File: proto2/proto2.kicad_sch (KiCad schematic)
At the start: 9 parts, among them J12 Daughter Card, SW1 SW_DIP_x04

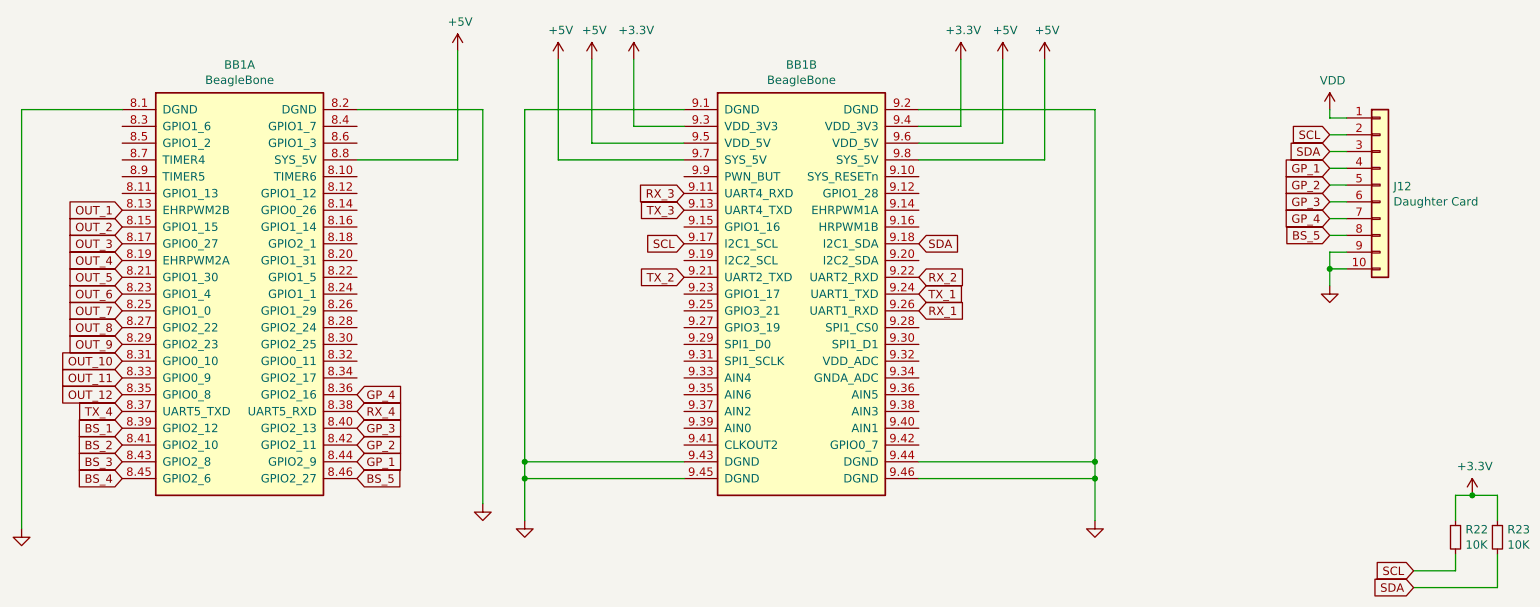
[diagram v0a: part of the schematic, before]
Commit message: Added another 2 outputs and re-routed board.
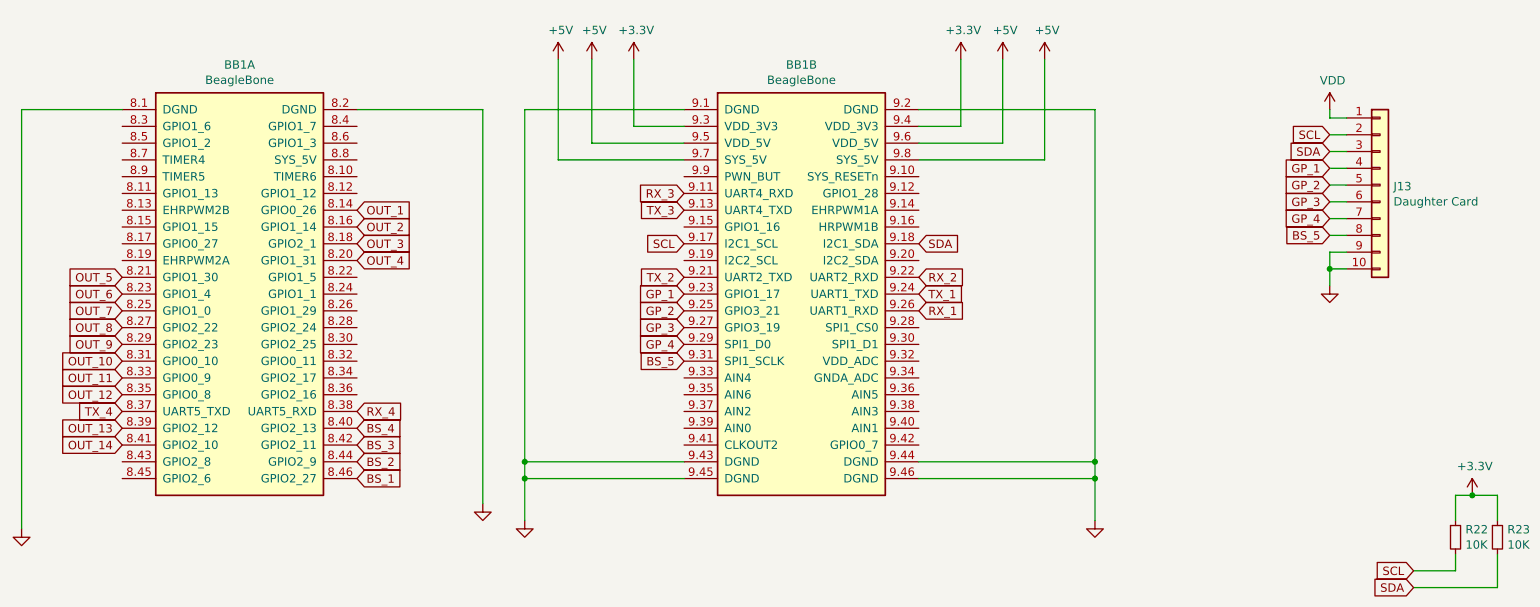
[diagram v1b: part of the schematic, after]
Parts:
- renumbered J12 to J13
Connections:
- net +5V: no longer BB1.8.8 (SYS_5V)
- net BS_1: now also BB1.8.46 (GPIO2_27); no longer BB1.8.39 (GPIO2_12)
- net BS_2: now also BB1.8.44 (GPIO2_9); no longer BB1.8.41 (GPIO2_10)
- net BS_3: now also BB1.8.42 (GPIO2_11); no longer BB1.8.43 (GPIO2_8)
- net BS_4: now also BB1.8.40 (GPIO2_13); no longer BB1.8.45 (GPIO2_6)
- net BS_5: now also BB1.9.31 (SPI1_SCLK); no longer BB1.8.46 (GPIO2_27)
- net GP_1: now also BB1.9.23 (GPIO1_17); no longer BB1.8.44 (GPIO2_9)
- net GP_2: now also BB1.9.25 (GPIO3_21); no longer BB1.8.42 (GPIO2_11)
- net GP_3: now also BB1.9.27 (GPIO3_19); no longer BB1.8.40 (GPIO2_13)
- net GP_4: now also BB1.9.29 (SPI1_D0); no longer BB1.8.36 (GPIO2_16)
- net OUT_1: now also BB1.8.14 (GPIO0_26); no longer BB1.8.13 (EHRPWM2B)
- net OUT_2: now also BB1.8.16 (GPIO1_14); no longer BB1.8.15 (GPIO1_15)
- net OUT_3: now also BB1.8.18 (GPIO2_1); no longer BB1.8.17 (GPIO0_27)
- net OUT_4: now also BB1.8.20 (GPIO1_31); no longer BB1.8.19 (EHRPWM2A)
- new net OUT_13: BB1.8.39 (GPIO2_12)
- new net OUT_14: BB1.8.41 (GPIO2_10)

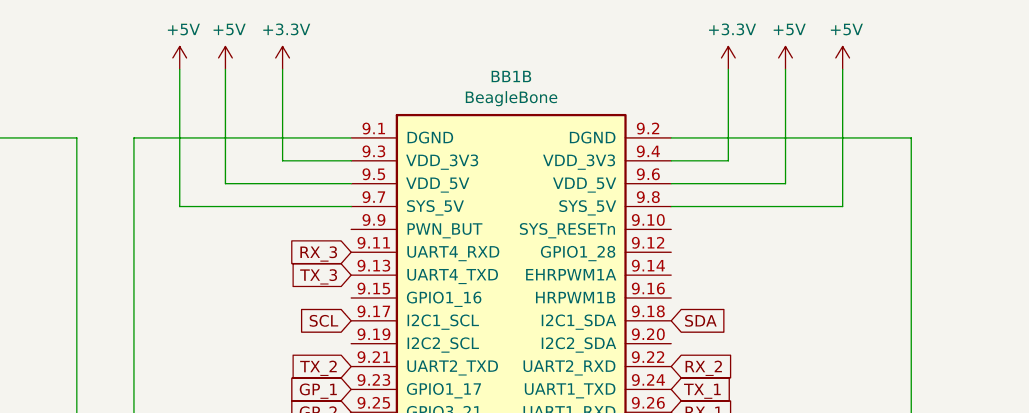
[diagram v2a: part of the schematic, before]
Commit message: Added switch for 5V external devices power based off SYS_RESETn.
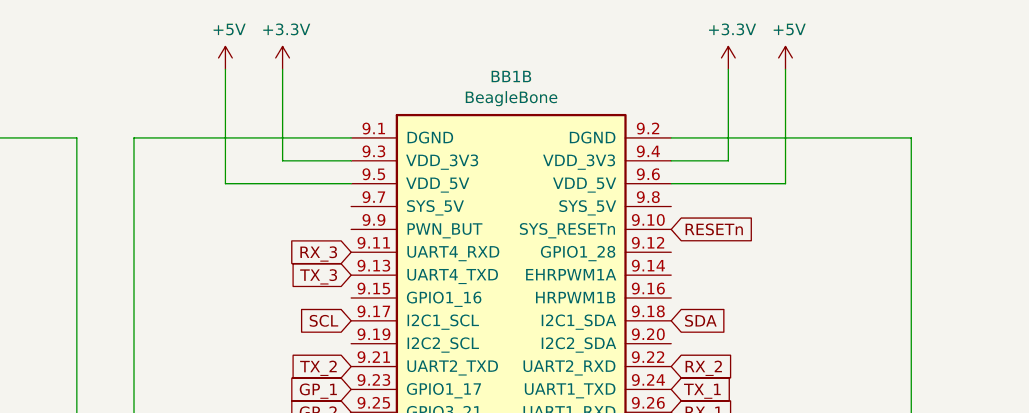
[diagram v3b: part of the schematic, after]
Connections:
- net +5V: no longer BB1.9.7 (SYS_5V), BB1.9.8 (SYS_5V)
- net RESETn: now reaches BB1.9.10 (SYS_RESETn)
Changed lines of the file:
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@@
-    (stroke (width 0) (type default) (color 0 0 0 0))
-  )
-  (wire (pts (xy 160.02 40.64) (xy 179.07 40.64))
     (stroke (width 0) (type default) (color 0 0 0 0))
   )
@@
     (stroke (width 0) (type default) (color 0 0 0 0))
   )
-  (wire (pts (xy 124.46 40.64) (xy 105.41 40.64))
-    (stroke (width 0) (type default) (color 0 0 0 0))
-  )
   (wire (pts (xy 224.79 36.83) (xy 222.25 36.83))
     (stroke (width 0) (type default) (color 0 0 0 0))
@@
     (stroke (width 0) (type default) (color 0 0 0 0))
   )
-  (wire (pts (xy 105.41 25.4) (xy 105.41 40.64))
-    (stroke (width 0) (type default) (color 0 0 0 0))
-  )
   (wire (pts (xy 193.04 137.16) (xy 198.12 137.16))
     (stroke (width 0) (type default) (color 0 0 0 0))
@@
   )
   (wire (pts (xy 214.63 125.73) (xy 214.63 120.65))
-    (stroke (width 0) (type default) (color 0 0 0 0))
-  )
-  (wire (pts (xy 179.07 40.64) (xy 179.07 25.4))
     (stroke (width 0) (type default) (color 0 0 0 0))
   )
@@
     (property "Intersheet References" "${INTERSHEET_REFS}" (id 0) (at 0 0 0)
       (effects (font (size 1.27 1.27)) hide)
+    )
+  )
+  (global_label "RESETn" (shape input) (at 160.02 43.18 0) (fields_autoplaced)
+    (effects (font (size 1.27 1.27)) (justify left))
+    (property "Intersheet References" "${INTERSHEET_REFS}" (id 0) (at 169.2385 43.1006 0)
+      (effects (font (size 1.27 1.27)) (justify left) hide)
     )
   )
@@
     (pin "1")
   )
-  (symbol (lib_id "power:+5V") (at 179.07 25.4 0) (unit 1)
-    (in_bom yes) (on_board yes)
-    (property "Reference" "#PWR07" (id 0) (at 179.07 29.21 0)
-      (effects (font (size 1.27 1.27)) hide)
-    )
-    (property "Value" "+5V" (id 1) (at 179.451 21.0058 0))
-    (property "Footprint" "" (id 2) (at 179.07 25.4 0)
-      (effects (font (size 1.27 1.27)) hide)
-    )
-    (property "Datasheet" "" (id 3) (at 179.07 25.4 0)
-      (effects (font (size 1.27 1.27)) hide)
-    )
-    (pin "1")
-  )
   (symbol (lib_id "power:+5V") (at 110.49 25.4 0) (unit 1)
     (in_bom yes) (on_board yes)
@@
     )
     (property "Datasheet" "" (id 3) (at 110.49 25.4 0)
-      (effects (font (size 1.27 1.27)) hide)
-    )
-    (pin "1")
-  )
-  (symbol (lib_id "power:+5V") (at 105.41 25.4 0) (unit 1)
-    (in_bom yes) (on_board yes)
-    (property "Reference" "#PWR02" (id 0) (at 105.41 29.21 0)
-      (effects (font (size 1.27 1.27)) hide)
-    )
-    (property "Value" "+5V" (id 1) (at 105.791 21.0058 0))
-    (property "Footprint" "" (id 2) (at 105.41 25.4 0)
-      (effects (font (size 1.27 1.27)) hide)
-    )
-    (property "Datasheet" "" (id 3) (at 105.41 25.4 0)
       (effects (font (size 1.27 1.27)) hide)
     )
@@
   )
   (symbol_instances
-    (path "/00000000-0000-0000-0000-000061bf4728"
-      (reference "#PWR02") (unit 1) (value "+5V") (footprint "")
+    (path "/00000000-0000-0000-0000-0000619eb672/a2db9d7b-b7f0-42c4-8bfa-d906fa3f908d"
+      (reference "#PWR01") (unit 1) (value "+5V") (footprint "")
+    )
+    (path "/00000000-0000-0000-0000-0000619eb672/1ea60411-14df-4e7e-a9fa-3b3b00f1524d"
+      (reference "#PWR02") (unit 1) (value "GND") (footprint "")
     )
     (path "/00000000-0000-0000-0000-000061bf42fc"
@@
       (reference "#PWR06") (unit 1) (value "+5V") (footprint "")
     )
-    (path "/00000000-0000-0000-0000-000061bf4113"
+    (path "/00000000-0000-0000-0000-0000619eb672/eaa45e24-ca48-404a-92a9-31cfd5b343bc"
       (reference "#PWR07") (unit 1) (value "+5V") (footprint "")
     )
@@
       (reference "#PWR079") (unit 1) (value "GNDPWR") (footprint "")
     )
+    (path "/00000000-0000-0000-0000-0000619eb672/e7637630-81e1-4c33-8f3d-d08d1824d6f6"
+      (reference "#PWR080") (unit 1) (value "+5VP") (footprint "")
+    )
     (path "/00000000-0000-0000-0000-0000619eb672/00000000-0000-0000-0000-000061cae676"
       (reference "#PWR096") (unit 1) (value "GNDPWR") (footprint "")
@@
       (reference "#PWR0109") (unit 1) (value "VDD") (footprint "")
     )
-    (path "/00000000-0000-0000-0000-0000619eb672/00000000-0000-0000-0000-000061daa2a5"
-      (reference "#PWR0110") (unit 1) (value "+5V") (footprint "")
-    )
     (path "/00000000-0000-0000-0000-0000619eb672/00000000-0000-0000-0000-000061ba8e74"
       (reference "#PWR0111") (unit 1) (value "GND") (footprint "")
@@
       (reference "#PWR0165") (unit 1) (value "Earth") (footprint "")
     )
+    (path "/00000000-0000-0000-0000-0000619eb672/b6c5cff6-cf86-4498-a76d-b9f56c83bf6b"
+      (reference "#PWR?") (unit 1) (value "+5VP") (footprint "")
+    )
     (path "/00000000-0000-0000-0000-000061b4e58b"
       (reference "BB1") (unit 1) (value "BeagleBone") (footprint "BCR_SBC:BeagleBone_UpsideDown")
@@
       (reference "Q14") (unit 1) (value "2N7002") (footprint "Package_TO_SOT_SMD:SOT-23")
     )
+    (path "/00000000-0000-0000-0000-0000619eb672/b660b5f4-a97d-4cf0-a5cf-f1705548cf79"
+      (reference "Q15") (unit 1) (value "2N7002") (footprint "Package_TO_SOT_SMD:SOT-23")
+    )
     (path "/00000000-0000-0000-0000-000061c509a6"
       (reference "R1") (unit 1) (value "10K") (footprint "Resistor_SMD:R_0805_2012Metric")
@@
       (reference "R54") (unit 1) (value "500R") (footprint "Capacitor_SMD:C_0805_2012Metric")
     )
+    (path "/00000000-0000-0000-0000-0000619eb672/5b1cfd4b-7b06-4f3f-8036-d9ad45660df3"
+      (reference "R55") (unit 1) (value "1K") (footprint "Resistor_SMD:R_0805_2012Metric")
+    )
+    (path "/00000000-0000-0000-0000-0000619eb672/22fe218f-cd70-40d4-84da-5b3454bd320a"
+      (reference "R56") (unit 1) (value "27K") (footprint "Resistor_SMD:R_0805_2012Metric")
+    )
+    (path "/00000000-0000-0000-0000-0000619eb672/ead9c149-9ccc-4416-b4a2-f88d2a070289"
+      (reference "R57") (unit 1) (value "433R") (footprint "Resistor_SMD:R_0805_2012Metric")
+    )
     (path "/00000000-0000-0000-0000-000061c44950"
       (reference "SW1") (unit 1) (value "SW_DIP_x04") (footprint "Button_Switch_BCR:CUI_DS04-254-2-04BK-SMT")
@@
       (reference "U15") (unit 1) (value "NCP59300") (footprint "Package_TO_SOT_SMD:TO-263-5_TabPin3")
     )
-  )
+    (path "/00000000-0000-0000-0000-0000619eb672/c38a8763-3e12-468f-b23a-66ca498566e0"
+      (reference "U16") (unit 1) (value "AQY282SX") (footprint "Package_SO:SO-4_4.4x4.3mm_P2.54mm")
+    )
+  )

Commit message: Working in suggestions from CFL review.
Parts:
- R22, R23: value 10K -> 4.7K; LCSC C17414 -> C17673
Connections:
- net iSCL: now reaches BB1.9.19 (I2C2_SCL)
- net iSCL: now also J13.2 (Pin_2), R22.2
- net iSDA: now reaches BB1.9.20 (I2C2_SDA)
- net iSDA: now also J13.3 (Pin_3), R23.2
- net RX_1 renamed iRX_1
- net RX_2 renamed iRX_2
- net RX_3 renamed iRX_3
- net RX_4: no longer names the net of BB1.8.38 (UART5_RXD)
- removed net SCL: BB1.9.17 (I2C1_SCL), J13.2 (Pin_2), R22.2
- removed net SDA: BB1.9.18 (I2C1_SDA), J13.3 (Pin_3), R23.2
- net TX_1 renamed iTX_1
- net TX_2 renamed iTX_2
- net TX_3 renamed iTX_3
- net TX_4: no longer names the net of BB1.8.37 (UART5_TXD)
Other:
- added sheet comms (comms.kicad_sch)

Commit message: Changes suggested by CFL.
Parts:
- added R21: 10K, Resistor_SMD:R_0805_2012Metric, symbol Device:R_Small
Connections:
- net +3V3: now also R21.1
- net BS_5: now also R21.2
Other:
- moved on the sheet: R22, R23

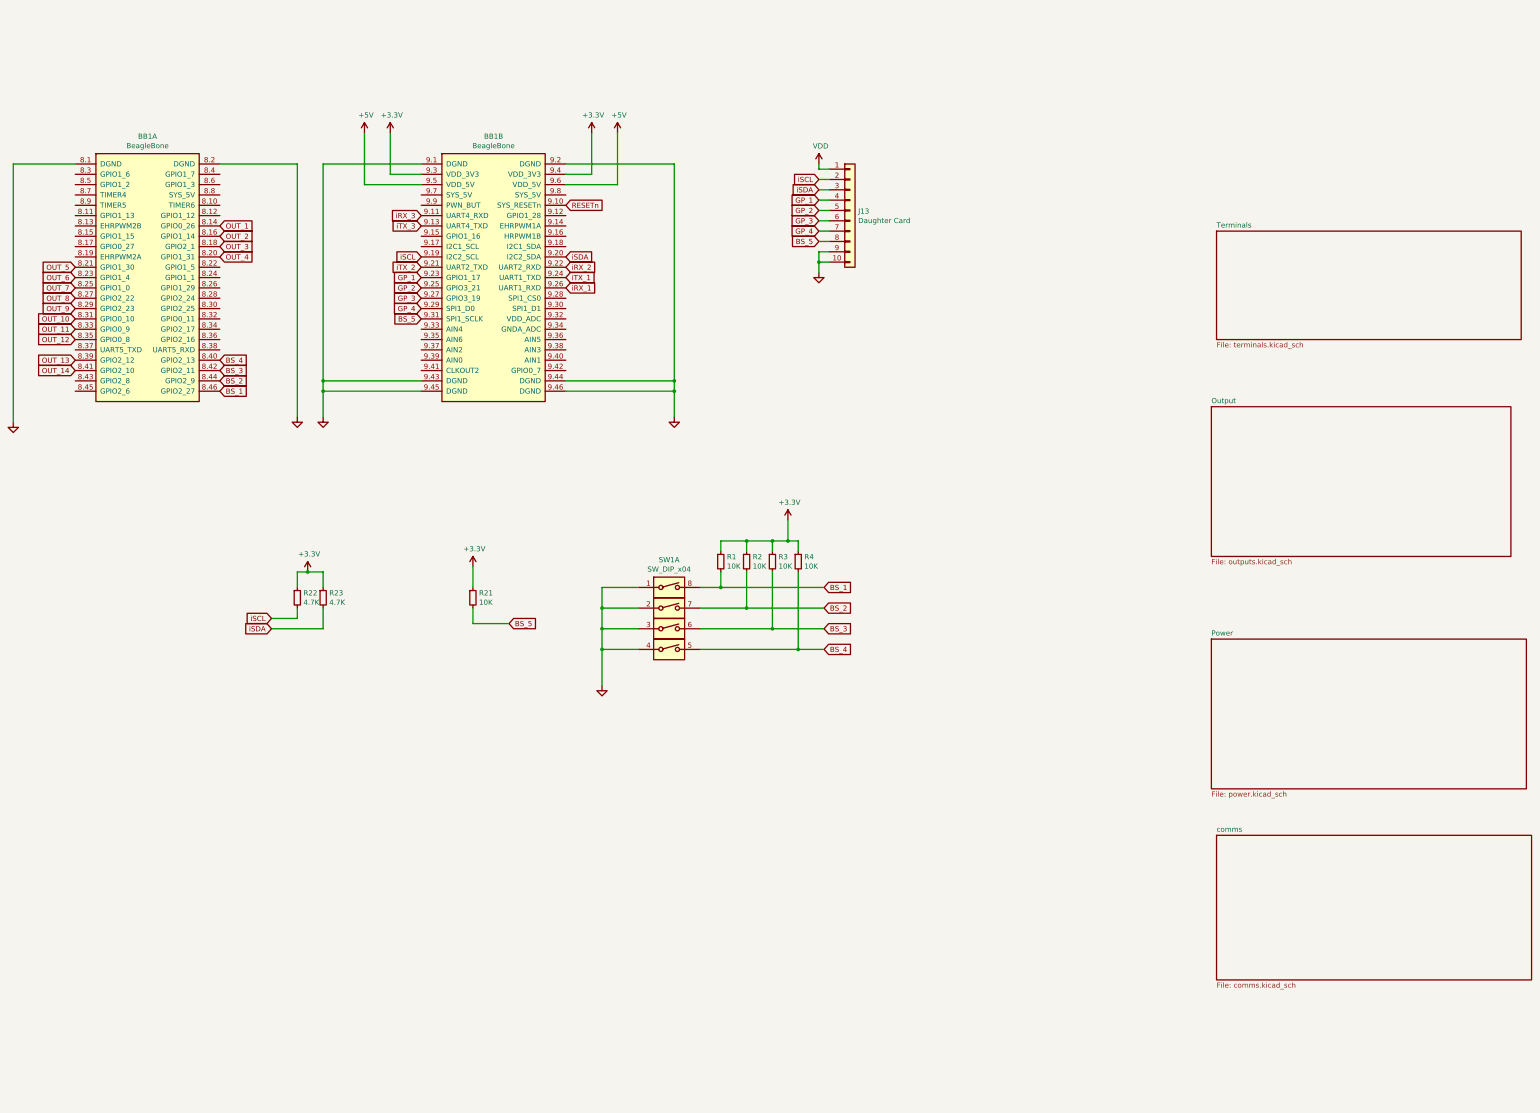
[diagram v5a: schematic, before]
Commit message: Laying out new filters and some schematic updates.
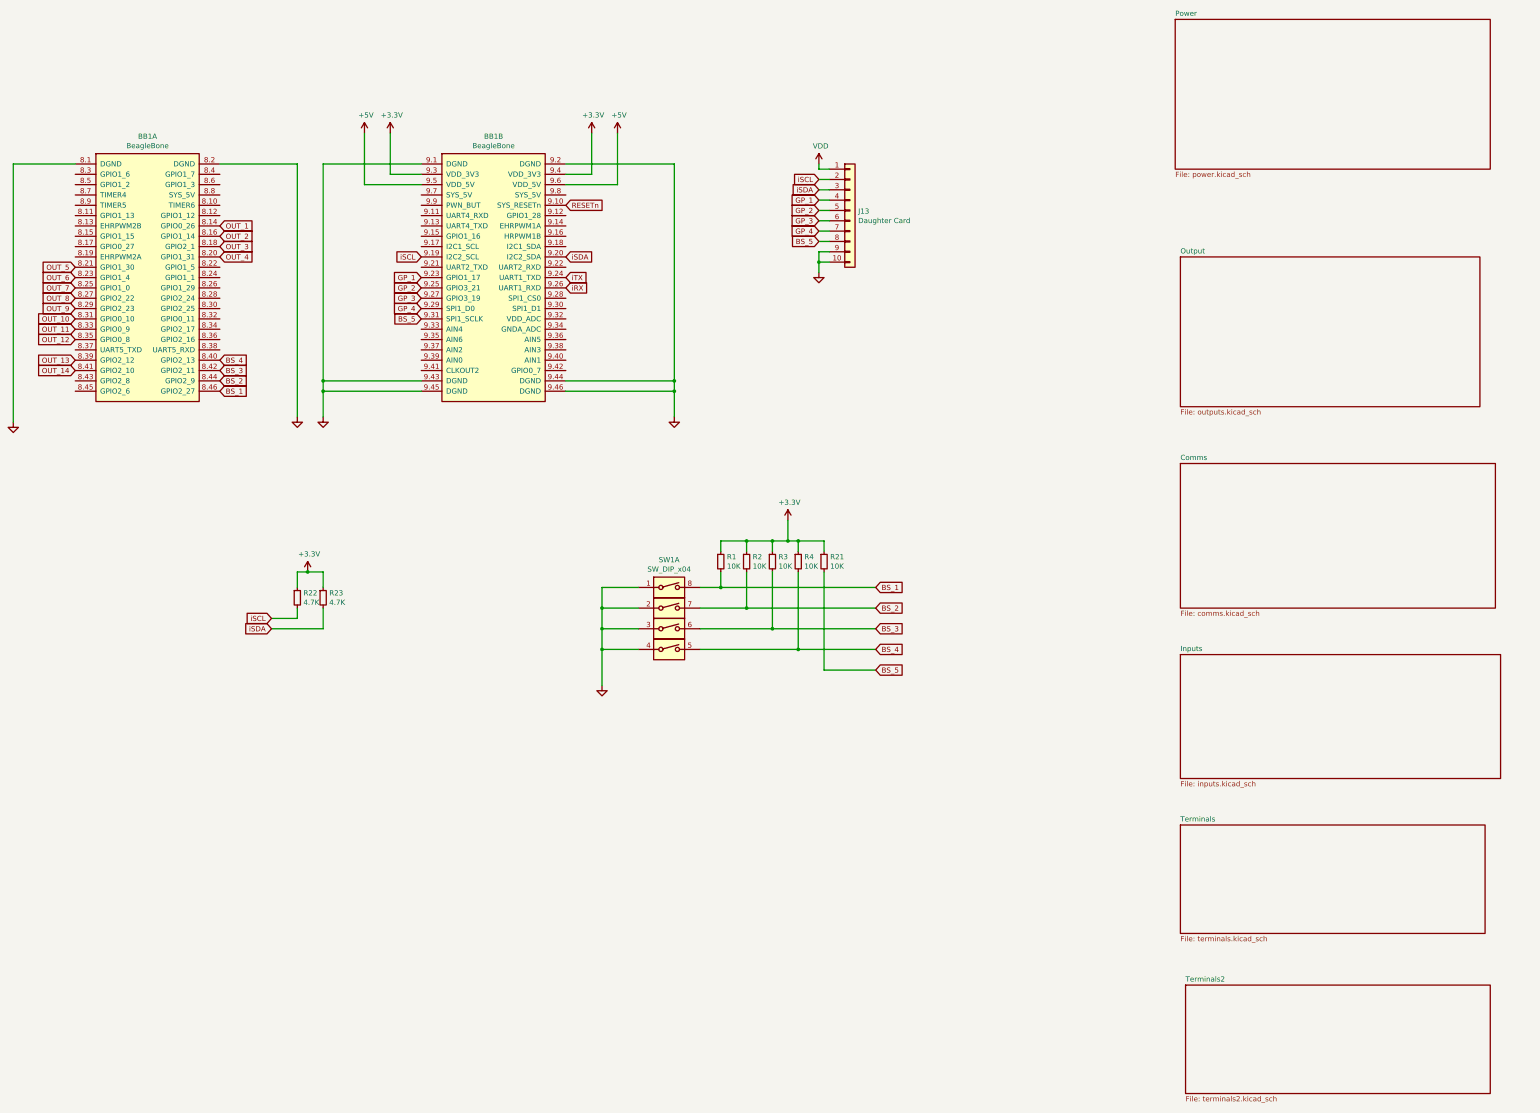
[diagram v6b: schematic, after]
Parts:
- J13: footprint Connector_PinHeader_2.54mm:PinHeader_1x10_P2.54mm_Vertical -> BCR_Langhe:Proto2_DaughterCard
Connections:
- net GND renamed GND-SIG
- net iRX_1 renamed iRX
- net iRX_2: no longer names the net of BB1.9.22 (UART2_RXD)
- net iRX_3: no longer names the net of BB1.9.11 (UART4_RXD)
- net iTX_1 renamed iTX
- net iTX_2: no longer names the net of BB1.9.21 (UART2_TXD)
- net iTX_3: no longer names the net of BB1.9.13 (UART4_TXD)
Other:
- sheet comms renamed Comms
- added sheet Inputs (inputs.kicad_sch)
- added sheet Terminals2 (terminals2.kicad_sch)
- moved on the sheet: R21
